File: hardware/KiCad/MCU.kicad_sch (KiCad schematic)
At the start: 88 parts, among them Q1 MMBF170, Q10 MMBF170, Q11 IRF9Z24S, Q12 MMBF170, Q13 MMBTA13, Q14 IRF9Z24S, Q15 MMBTA13, Q16 MMBF170, Q2 MMBF170, Q3 MMBF170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

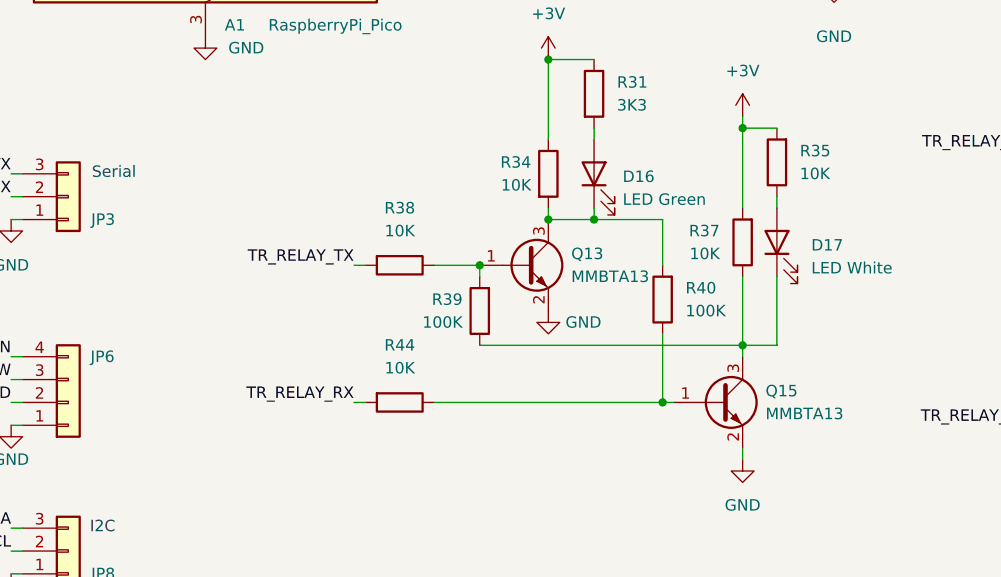
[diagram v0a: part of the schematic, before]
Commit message: Fixed circuit for latched relays
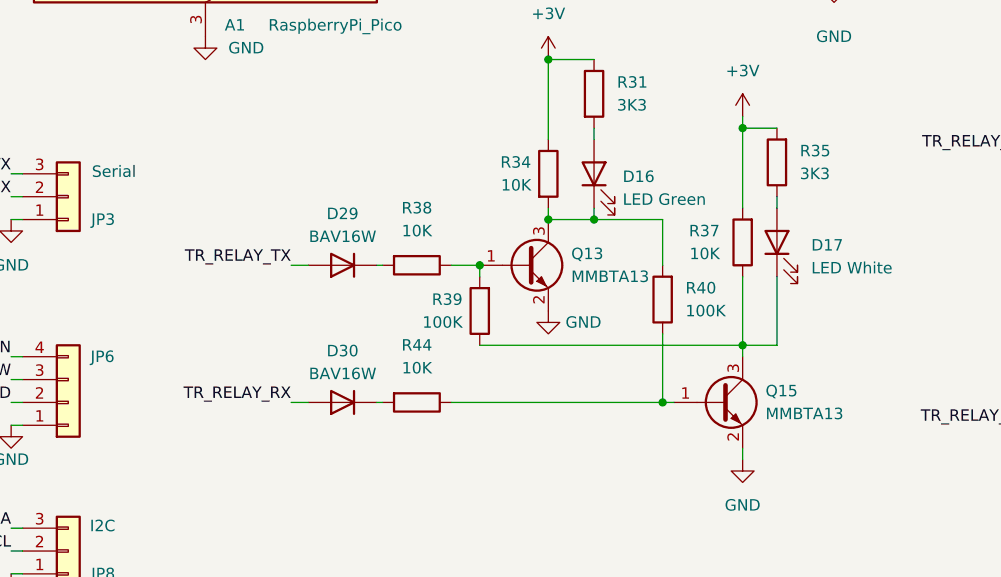
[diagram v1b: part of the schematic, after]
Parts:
- added D29, D30: BAV16W, Diode_SMD:D_SOD-323_HandSoldering, symbol Diode:BAV16W
- R35: value 10K -> 3K3
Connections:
- net TR_RELAY_RX: now also D30.2 (A); no longer R44.2
- net TR_RELAY_TX: now also D29.2 (A); no longer R38.2
- new net: D30.1 (K), R44.2
- new net: D29.1 (K), R38.2
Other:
- moved on the sheet: R38, R44
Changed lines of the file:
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@@
 	(wire
 		(pts
-			(xy 171.45 137.16) (xy 176.53 137.16)
+			(xy 173.355 137.16) (xy 176.53 137.16)
 		)
 		(stroke
@@
 	(wire
 		(pts
-			(xy 171.45 152.4) (xy 196.85 152.4)
+			(xy 173.355 152.4) (xy 196.85 152.4)
 		)
 		(stroke
@@
 	(wire
 		(pts
-			(xy 162.56 152.4) (xy 163.83 152.4)
+			(xy 165.1 152.4) (xy 165.735 152.4)
 		)
 		(stroke
@@
 	(wire
 		(pts
+			(xy 157.48 137.16) (xy 155.575 137.16)
+		)
+		(stroke
+			(width 0)
+			(type default)
+		)
+	)
+	(wire
+		(pts
 			(xy 241.3 48.26) (xy 243.84 48.26)
 		)
@@
 	(wire
 		(pts
+			(xy 157.48 152.4) (xy 155.575 152.4)
+		)
+		(stroke
+			(width 0)
+			(type default)
+		)
+	)
+	(wire
+		(pts
 			(xy 207.01 48.26) (xy 223.52 48.26)
 		)
@@
 	(wire
 		(pts
-			(xy 162.56 137.16) (xy 163.83 137.16)
+			(xy 165.1 137.16) (xy 165.735 137.16)
 		)
 		(stroke
@@
 	)
 	(label "TR_RELAY_TX"
-		(at 162.56 137.16 180)
+		(at 155.575 137.16 180)
 		(effects
 			(font
@@
 	)
 	(label "TR_RELAY_RX"
-		(at 162.56 152.4 180)
+		(at 155.575 152.4 180)
 		(effects
 			(font
@@
 	(symbol
 		(lib_id "Device:R")
-		(at 167.64 152.4 270)
+		(at 169.545 152.4 270)
 		(unit 1)
 		(exclude_from_sim no)
@@
 		(fields_autoplaced yes)
 		(property "Reference" "R44"
-			(at 167.64 146.05 90)
+			(at 169.545 146.05 90)
 			(effects
 				(font
@@
 		)
 		(property "Value" "10K"
-			(at 167.64 148.59 90)
+			(at 169.545 148.59 90)
 			(effects
 				(font
@@
 		)
 		(property "Footprint" "Resistor_SMD:R_0805_2012Metric_Pad1.20x1.40mm_HandSolder"
-			(at 167.64 150.622 90)
+			(at 169.545 150.622 90)
 			(effects
 				(font
@@
 		)
 		(property "Datasheet" "~"
-			(at 167.64 152.4 0)
+			(at 169.545 152.4 0)
 			(effects
 				(font
@@
 		)
 		(property "Description" "Resistor"
-			(at 167.64 152.4 0)
+			(at 169.545 152.4 0)
 			(effects
 				(font
@@
 			)
 		)
-		(property "Value" "10K"
+		(property "Value" "3K3"
 			(at 212.09 126.9999 0)
 			(effects
@@
 	)
 	(symbol
+		(lib_id "Diode:BAV16W")
+		(at 161.29 152.4 180)
+		(unit 1)
+		(exclude_from_sim no)
+		(in_bom yes)
+		(on_board yes)
+		(dnp no)
+		(fields_autoplaced yes)
+		(property "Reference" "D30"
+			(at 161.29 146.685 0)
+			(effects
+				(font
+					(size 1.27 1.27)
+				)
+			)
+		)
+		(property "Value" "BAV16W"
+			(at 161.29 149.225 0)
+			(effects
+				(font
+					(size 1.27 1.27)
+				)
+			)
+		)
+		(property "Footprint" "Diode_SMD:D_SOD-323_HandSoldering"
+			(at 161.29 147.955 0)
+			(effects
+				(font
+					(size 1.27 1.27)
+				)
+				(hide yes)
+			)
+		)
+		(property "Datasheet" "https://www.diodes.com/assets/Datasheets/ds30086.pdf"
+			(at 161.29 152.4 0)
+			(effects
+				(font
+					(size 1.27 1.27)
+				)
+				(hide yes)
+			)
+		)
+		(property "Description" "75V 0.15A Fast Switching Diode, SOD-123"
+			(at 161.29 152.4 0)
+			(effects
+				(font
+					(size 1.27 1.27)
+				)
+				(hide yes)
+			)
+		)
+		(property "Sim.Device" "D"
+			(at 161.29 152.4 0)
+			(effects
+				(font
+					(size 1.27 1.27)
+				)
+				(hide yes)
+			)
+		)
+		(property "Sim.Pins" "1=K 2=A"
+			(at 161.29 152.4 0)
+			(effects
+				(font
+					(size 1.27 1.27)
+				)
+				(hide yes)
+			)
+		)
+		(pin "1"
+		)
+		(pin "2"
+		)
+		(instances
+			(project ""
+				(path "/74990c44-c45c-483c-b9bf-47d3ef73d6b4/723da1c1-8e54-42fb-a8a1-049649dc1b24"
+					(reference "D30")
+					(unit 1)
+				)
+			)
+		)
+	)
+	(symbol
 		(lib_id "power:GND")
 		(at 92.71 31.75 0)
@@
 	(symbol
 		(lib_id "Device:R")
-		(at 167.64 137.16 270)
+		(at 169.545 137.16 270)
 		(unit 1)
 		(exclude_from_sim no)
@@
 		(fields_autoplaced yes)
 		(property "Reference" "R38"
-			(at 167.64 130.81 90)
+			(at 169.545 130.81 90)
 			(effects
 				(font
@@
 		)
 		(property "Value" "10K"
-			(at 167.64 133.35 90)
+			(at 169.545 133.35 90)
 			(effects
 				(font
@@
 		)
 		(property "Footprint" "Resistor_SMD:R_0805_2012Metric_Pad1.20x1.40mm_HandSolder"
-			(at 167.64 135.382 90)
+			(at 169.545 135.382 90)
 			(effects
 				(font
@@
 		)
 		(property "Datasheet" "~"
-			(at 167.64 137.16 0)
+			(at 169.545 137.16 0)
 			(effects
 				(font
@@
 		)
 		(property "Description" "Resistor"
-			(at 167.64 137.16 0)
+			(at 169.545 137.16 0)
 			(effects
 				(font
@@
 					(unit 1)
 				)
+			)
+		)
+	)
+	(symbol
+		(lib_id "Diode:BAV16W")
+		(at 161.29 137.16 180)
+		(unit 1)
+		(exclude_from_sim no)
+		(in_bom yes)
+		(on_board yes)
+		(dnp no)
+		(fields_autoplaced yes)
+		(property "Reference" "D29"
+			(at 161.29 131.445 0)
+			(effects
+				(font
+					(size 1.27 1.27)
+				)
+			)
+		)
+		(property "Value" "BAV16W"
+			(at 161.29 133.985 0)
+			(effects
+				(font
+					(size 1.27 1.27)
+				)
+			)
+		)
+		(property "Footprint" "Diode_SMD:D_SOD-323_HandSoldering"
+			(at 161.29 132.715 0)
+			(effects
+				(font
+					(size 1.27 1.27)
+				)
+				(hide yes)
+			)
+		)
+		(property "Datasheet" "https://www.diodes.com/assets/Datasheets/ds30086.pdf"
+			(at 161.29 137.16 0)
+			(effects
+				(font
+					(size 1.27 1.27)
+				)
+				(hide yes)
+			)
+		)
+		(property "Description" "75V 0.15A Fast Switching Diode, SOD-123"
+			(at 161.29 137.16 0)
+			(effects
+				(font
+					(size 1.27 1.27)
+				)
+				(hide yes)
+			)
+		)
+		(property "Sim.Device" "D"
+			(at 161.29 137.16 0)
+			(effects
+				(font
+					(size 1.27 1.27)
+				)
+				(hide yes)
+			)
+		)
+		(property "Sim.Pins" "1=K 2=A"
+			(at 161.29 137.16 0)
+			(effects
+				(font
+					(size 1.27 1.27)
+				)
+				(hide yes)
+			)
+		)
+		(pin "1"
+		)
+		(pin "2"
+		)
+		(instances
+			(project ""
+				(path "/74990c44-c45c-483c-b9bf-47d3ef73d6b4/723da1c1-8e54-42fb-a8a1-049649dc1b24"
+					(reference "D29")
+					(unit 1)
+				)
